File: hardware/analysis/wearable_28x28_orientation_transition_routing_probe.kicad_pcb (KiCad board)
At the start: 4 copper layers, 61.2 x 61.2 mm, 784 parts

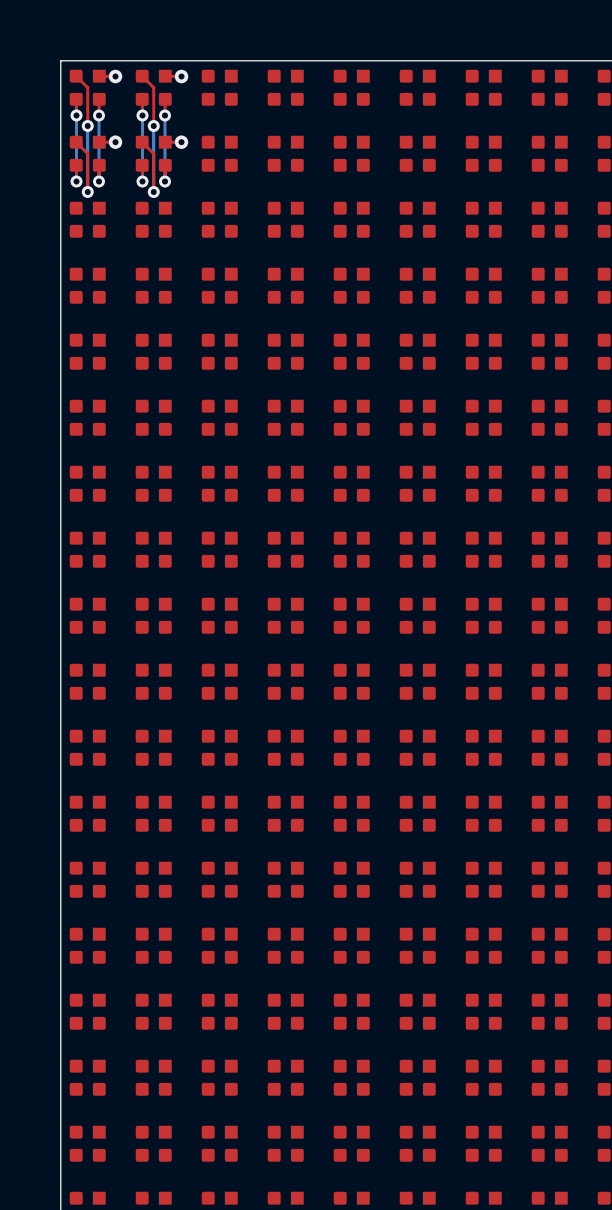
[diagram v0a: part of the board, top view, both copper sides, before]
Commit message: Validate matrix orientation transition routing
Co-authored-by: illiapliukhin <illiapliukhin@users.noreply.github.com>
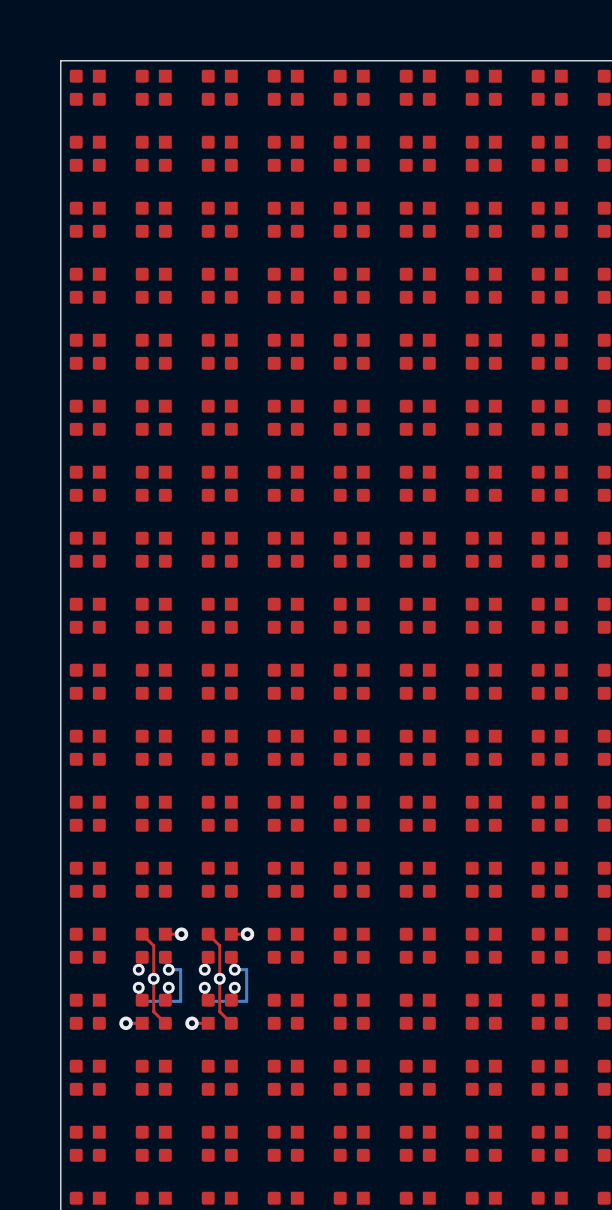
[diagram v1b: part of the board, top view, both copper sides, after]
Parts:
- turned D394 to 180 degrees
- turned D395 to 180 degrees
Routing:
- net COL_B_01: track 5.84 -> 0.00 mm, vias 2 -> 0
- net COL_G_03: track 0.00 -> 4.16 mm, vias 0 -> 2
- net COL_R_03: track 0.00 -> 4.16 mm, vias 0 -> 2
- net ROW_02_ANODE: track 4.05 -> 0.00 mm, vias 2 -> 0
- net ROW_14_ANODE: track 0.00 -> 4.05 mm, vias 0 -> 2
- net ROW_15_ANODE: track 0.00 -> 4.05 mm, vias 0 -> 2
- net COL_B_03: track 0.00 -> 3.49 mm, vias 0 -> 1
- net COL_R_01: track 3.28 -> 0.00 mm, vias 2 -> 0
- net COL_G_01: track 3.28 -> 0.00 mm, vias 2 -> 0
- net ROW_01_ANODE: track 3.28 -> 0.00 mm, vias 2 -> 0
- net COL_B_02: track 5.84 -> 3.49 mm, vias 2 -> 1
- net COL_R_02: track 3.28 -> 4.16 mm
- net COL_G_02: track 3.28 -> 4.16 mm
